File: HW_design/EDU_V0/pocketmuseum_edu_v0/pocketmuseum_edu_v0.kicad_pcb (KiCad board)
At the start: 4 copper layers, 96.8 x 51 mm, 106 parts, among them J101 USB_C_Receptacle_USB2.0_16P, J102 JST PH S2B, J201 TF-015, J205 BM04B-SRSS-TB, J206 BM04B-SRSS-TB, Q301 BSS138, Q302 BSS138, Q303 BSS138, SW101 PTS810SJG250, SW201 PTS810SJG250, U101 BQ24040, U102 APX803-29SAG, U103 AP2112K-3.3, U104 AP2112K-1.8, U201 ESP32-C6-MINI-1/U, U301 ICM-20948, U302 ICP20100, U303 BH1750FVI, U304 T3902

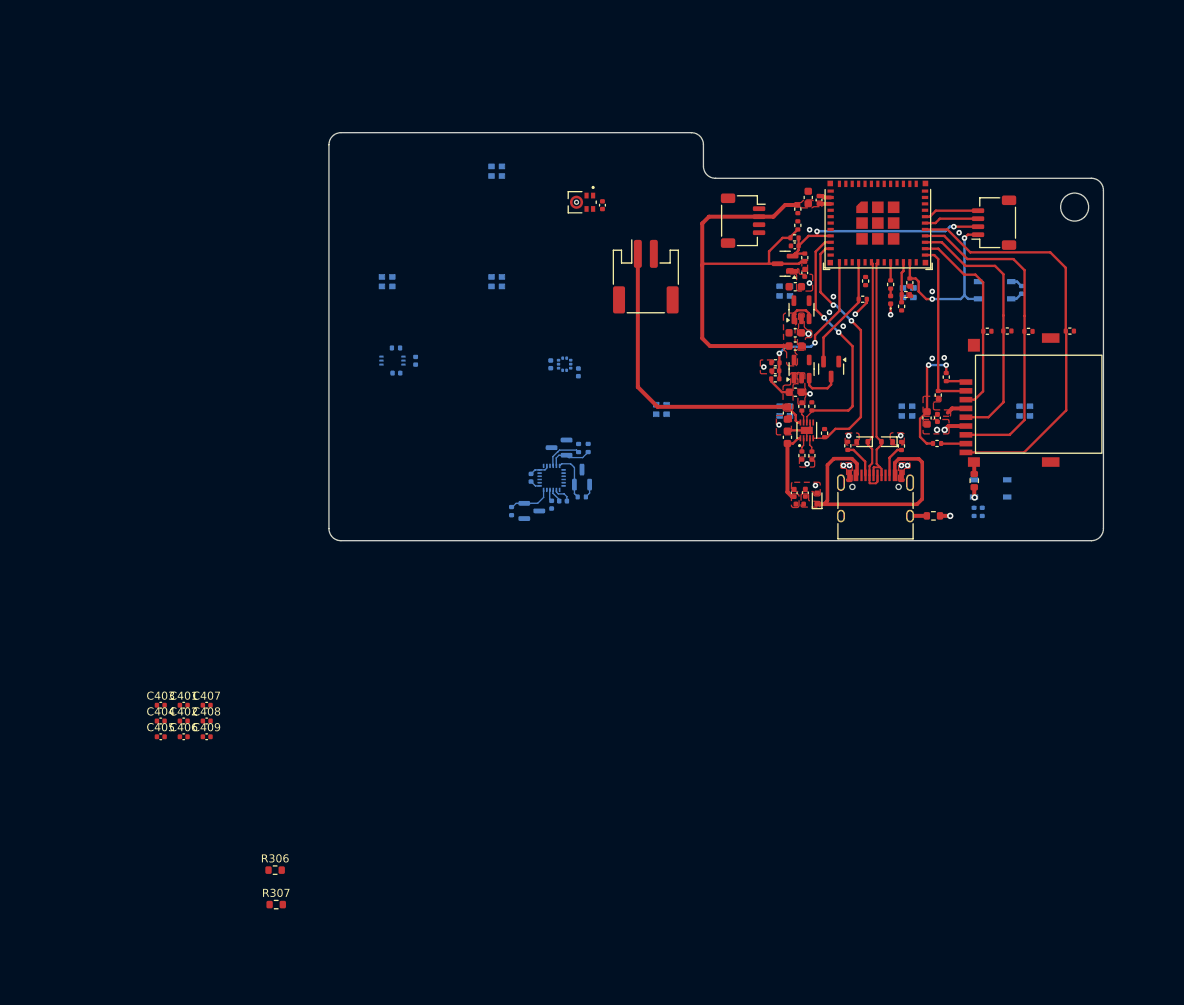
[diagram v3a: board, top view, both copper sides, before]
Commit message: EDU V0 PCB Placement Complete
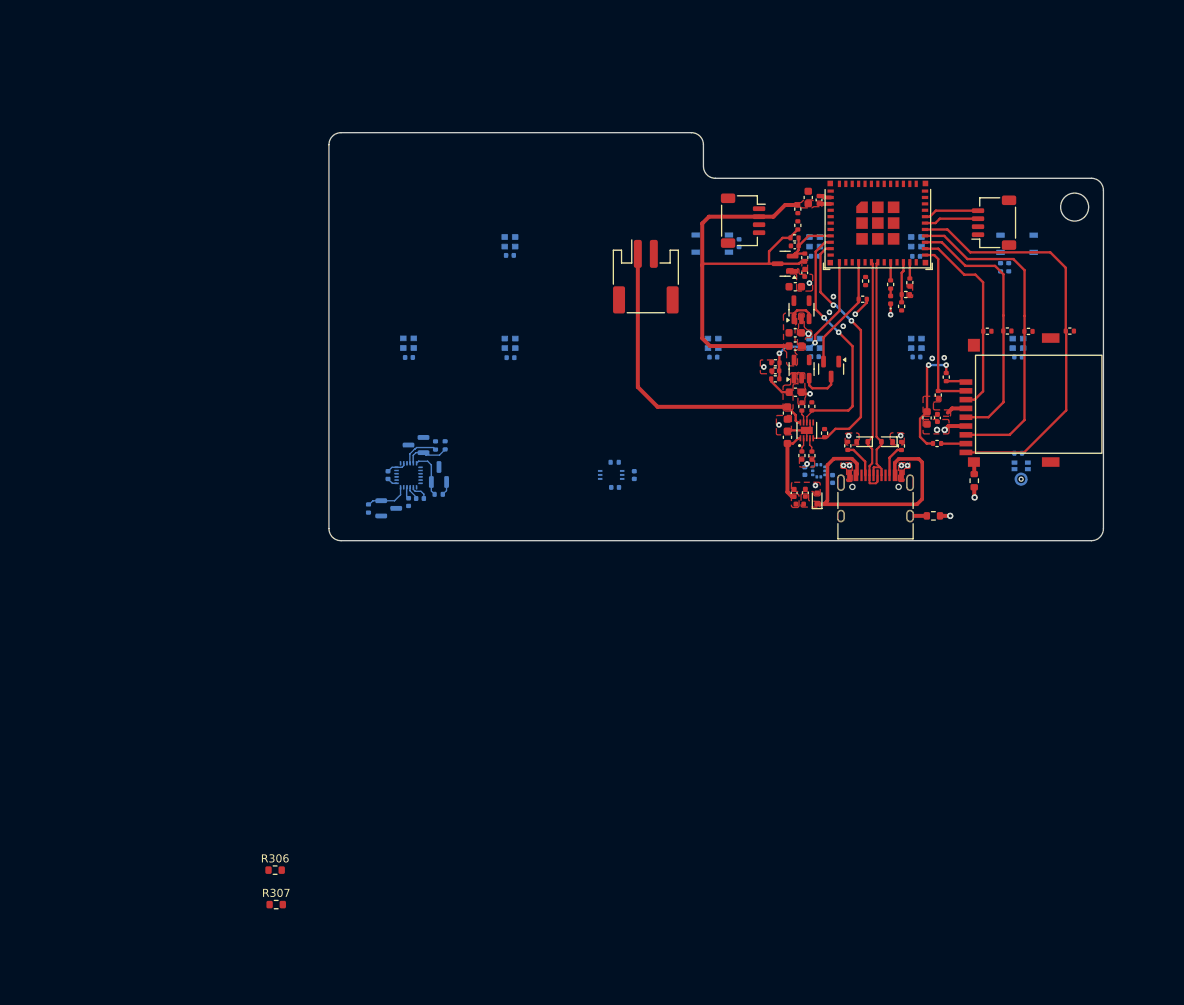
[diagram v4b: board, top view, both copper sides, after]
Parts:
- C308, C401, C402, C403, C404, C405, C406, C407, C408, C409, U304: moved to B.Cu
- moved C409 112.0 mm to (183.9, 93.8), turned to 180 degrees
- moved C401 107.4 mm to (171.2, 81.3), turned to 180 degrees
- moved C408 99.7 mm to (171.2, 93.8), turned to 180 degrees
- moved C402 98.0 mm to (158.5, 81.2), turned to 180 degrees
- moved C407 87.6 mm to (158.5, 93.8), turned to 180 degrees
- moved C406 81.5 mm to (145.8, 93.9), turned to 180 degrees
- moved D409 79.2 mm to (183.3, 96.3)
- moved C403 71.2 mm to (120.4, 81.1), turned to 180 degrees
- moved U304 64.5 mm to (184.3, 108.4), turned to 180 degrees
- moved C405 64.5 mm to (120.5, 93.9), turned to 180 degrees
- moved C308 60.5 mm to (183.9, 105.9), turned to 0 degrees
- moved C404 55.0 mm to (107.8, 93.9), turned to 180 degrees
- moved D403 54.0 mm to (119.8, 83.6)
- moved D408 53.0 mm to (170.6, 96.3)
- moved D404 47.8 mm to (107.1, 96.3)
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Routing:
- net /MCU/STRAP_GPIO_9: track 23.3 -> 2.03 mm, vias 2 -> 0
- net CHIP_PU: track 29.7 -> 8.77 mm, vias 2 -> 0
- net GND: track 22.9 -> 21.4 mm, vias 27 -> 24

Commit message: EDUV0 HW Complete Placement
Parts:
- added H2: MountingHole, MountingHole:MountingHole_3.2mm_M3, F.Cu at (101.2, 113.4)
- added H3: MountingHole, MountingHole:MountingHole_3.2mm_M3, F.Cu at (101.2, 69.2)
- added H4: MountingHole, MountingHole:MountingHole_3.2mm_M3, F.Cu at (191.2, 113.3)
- H1: footprint MountingHole:MountingHole_3.5mm -> MountingHole:MountingHole_3.2mm_M3
- moved SW101 50.7 mm to (133.9, 71.0), turned to -90 degrees
- moved R112 47.2 mm to (136.8, 72.0), turned to 0 degrees
- moved R111 45.9 mm to (136.8, 73.0), turned to 180 degrees
- moved SW201 38.1 mm to (183.8, 80.1), turned to 90 degrees
- moved C203 35.0 mm to (183.9, 83.4), turned to 0 degrees
- moved R304 9.22 mm to (111.9, 113.0), turned to 180 degrees
- moved R301 8.38 mm to (104.0, 103.5), turned to 0 degrees
- moved R305 7.05 mm to (104.1, 104.7), turned to 0 degrees
- moved Q303 7.03 mm to (111.9, 110.5), turned to 90 degrees
- moved R302 6.88 mm to (110.2, 104.3), turned to -90 degrees
- moved Q301 5.77 mm to (107.7, 104.2), turned to 180 degrees
- moved C303 5.21 mm to (111.1, 108.0), turned to 180 degrees
- moved Q302 5.18 mm to (104.0, 107.1), turned to -90 degrees
- moved C301 5.16 mm to (110.7, 106.6), turned to -90 degrees
- moved C302 3.28 mm to (107.8, 110.6), turned to 0 degrees
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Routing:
- net BATT_VOLT_FDBCK: track 19.5 -> 10.5 mm, vias 2 -> 1

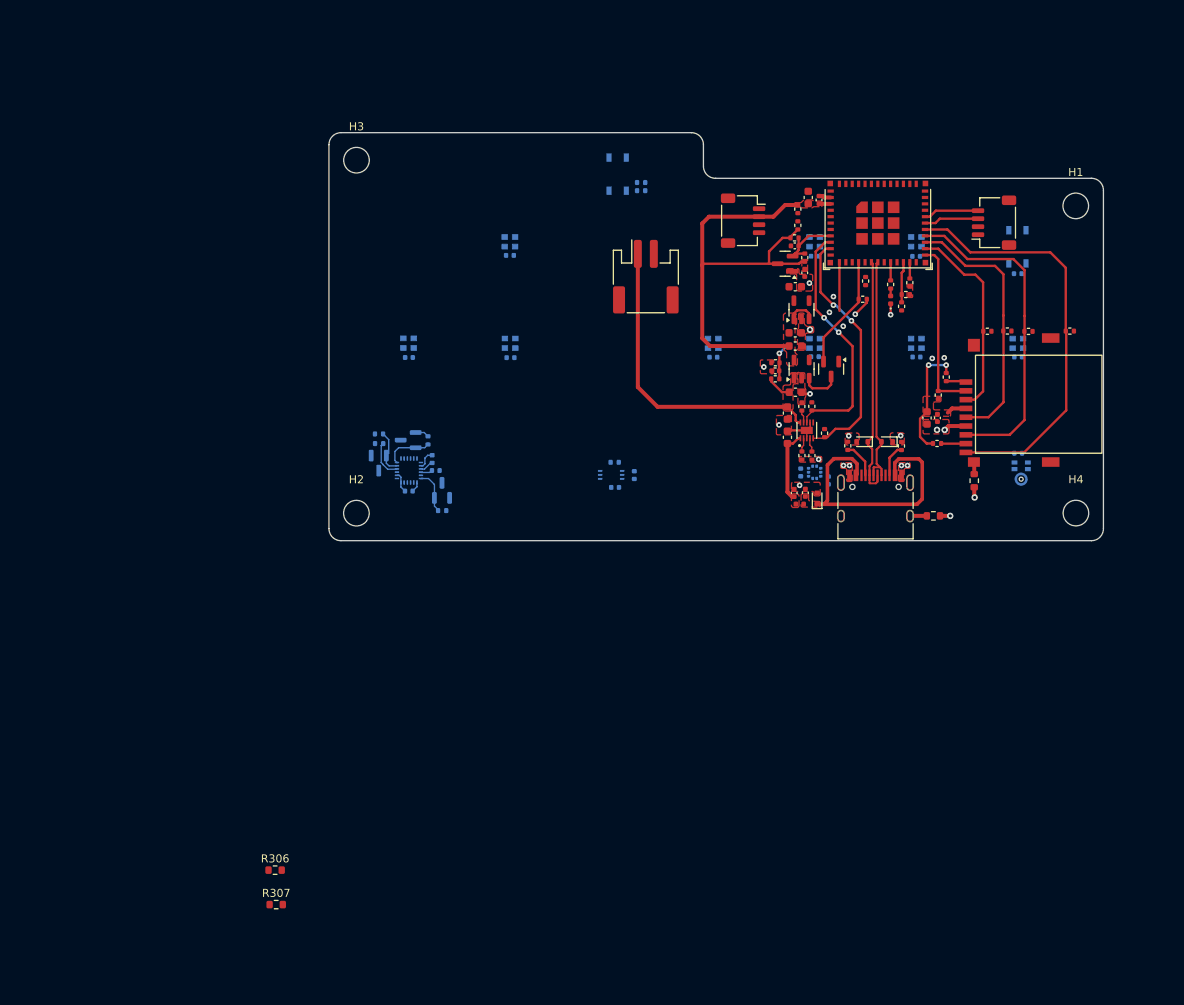
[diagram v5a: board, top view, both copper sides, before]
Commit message: EDUV0 added TP n routing in progress
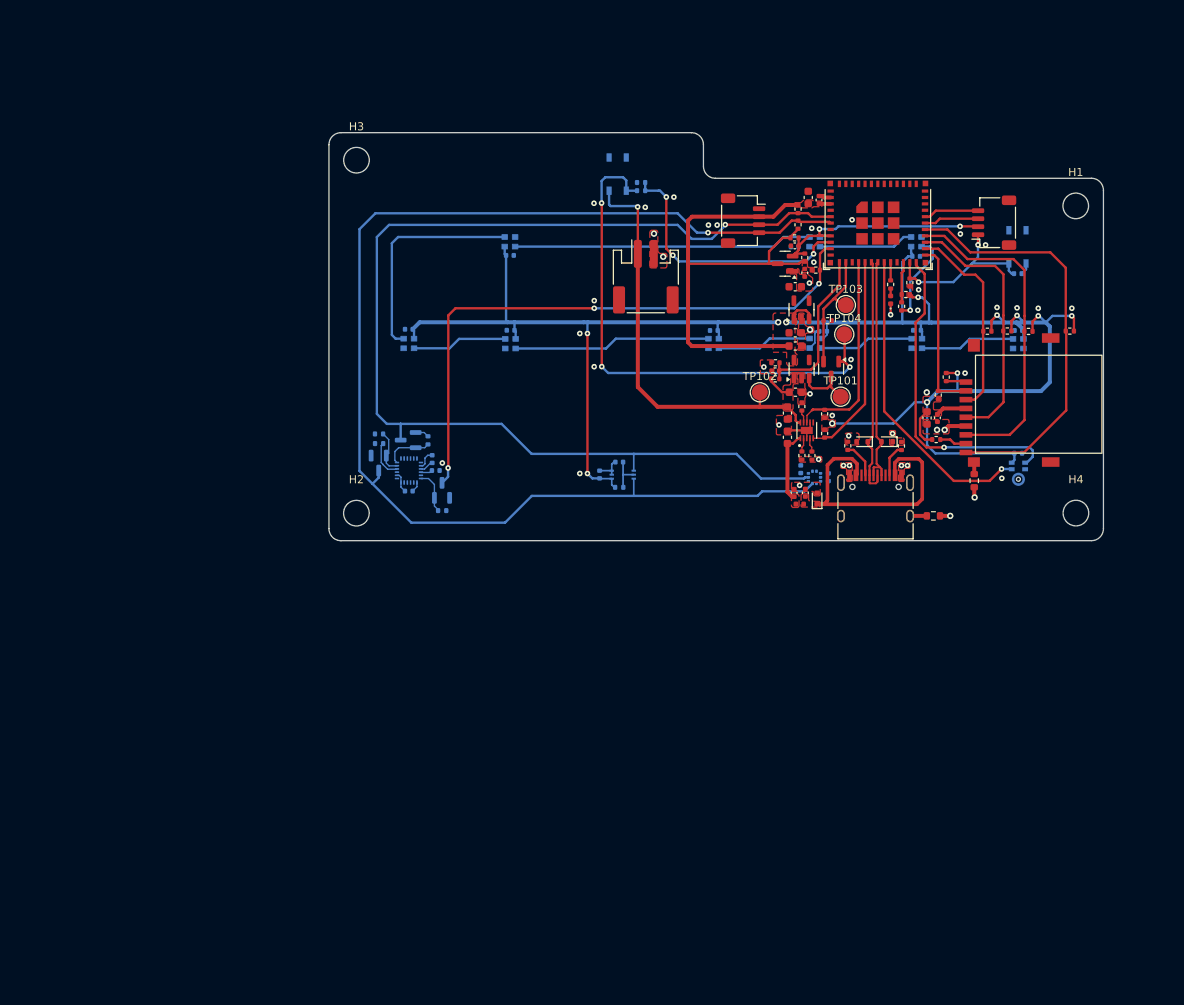
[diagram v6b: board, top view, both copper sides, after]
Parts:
- removed R306, R307: 0R, Resistor_SMD:R_0603_1608Metric
- added TP101: TestPoint, TestPoint:TestPoint_Pad_D2.0mm, F.Cu at (161.8, 98.8)
- added TP102: TestPoint, TestPoint:TestPoint_Pad_D2.0mm, F.Cu at (151.7, 98.2)
- added TP103: TestPoint, TestPoint:TestPoint_Pad_D2.0mm, F.Cu at (162.4, 87.3)
- added TP104: TestPoint, TestPoint:TestPoint_Pad_D2.0mm, F.Cu at (162.2, 91.0)
- moved D407 8.52 mm to (159.2, 87.9), turned to 0 degrees
- moved D406 8.50 mm to (146.5, 88.0), turned to 0 degrees
- moved D408 8.50 mm to (171.9, 88.0), turned to 0 degrees
- moved D409 8.47 mm to (184.6, 88.0), turned to 0 degrees
- moved D404 8.47 mm to (108.4, 88.0), turned to 0 degrees
- moved D405 8.46 mm to (121.1, 88.0), turned to 0 degrees
- moved R303 6.37 mm to (158.7, 83.0), turned to 0 degrees
- moved R113 5.14 mm to (160.1, 89.3)
- moved C306 4.34 mm to (131.6, 108.5), turned to 90 degrees
- moved C305 3.73 mm to (156.8, 107.9), turned to -90 degrees
- moved C404 3.53 mm to (107.8, 90.4), turned to 0 degrees
- moved C304 3.51 mm to (160.2, 108.9), turned to 90 degrees
- moved C405 3.42 mm to (120.5, 90.5), turned to 0 degrees
- moved C408 3.34 mm to (171.3, 90.5), turned to 0 degrees
- moved C406 3.34 mm to (145.9, 90.5), turned to 0 degrees
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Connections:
- U201 pad 10: BATT_POWOK_FDBCK -> MEMS_INT
- U201 pad 13: BATT_SW_FDBCK -> BATT_ATTCH_CMD
- U201 pad 15: BATT_ATTCH_CMD -> BATT_CHRG_FDBCK
- U201 pad 16: MEMS_INT -> BATT_POWOK_FDBCK
- U201 pad 5: I2C_SCL -> I2C_SDA
- U201 pad 6: I2C_SDA -> I2C_SCL
- U201 pad 9: BATT_CHRG_FDBCK -> BATT_SW_FDBCK
- U302 pad 2: Net-(U302-SCL) -> I2C_SCL
- U302 pad 4: Net-(U302-SDA) -> I2C_SDA
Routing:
- net +3V3: track 80.0 -> 293.7 mm, vias 2 -> 12
- net I2C_SCL: track 0.00 -> 157.1 mm, vias 0 -> 1
- net I2C_SDA: track 0.00 -> 143.2 mm, vias 0 -> 1
- net MEMS_INT: track 0.00 -> 74.6 mm, vias 0 -> 3
- net /Power/BATT_SW_CMD: track 0.00 -> 66.2 mm, vias 0 -> 3
- net I2S_DAT: track 0.00 -> 40.1 mm, vias 0 -> 1
- net I2S_CLK: track 0.00 -> 38.8 mm, vias 0 -> 1
- net /Feedback/WS2812B_Chain2: track 0.00 -> 37.3 mm
- net BATT_SW_FDBCK: track 0.00 -> 33.2 mm, vias 0 -> 3
- net /Feedback/WS2812B_Chain3: track 0.00 -> 27.6 mm
- net /Feedback/WS2812B_Chain5: track 0.00 -> 24.6 mm
- net CHIP_PU: track 8.77 -> 31.0 mm, vias 0 -> 2
- net /MCU/STRAP_GPIO_9: track 2.03 -> 21.2 mm, vias 0 -> 2
- net VBAT_ALW_ON: track 42.3 -> 55.4 mm, vias 0 -> 1
- net /Feedback/WS2812B_Chain7: track 0.00 -> 11.9 mm
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
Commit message: EDUV0 signals & 3V3 traces COMPLETE
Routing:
- net +3V3: track 293.7 -> 321.2 mm, vias 12 -> 13
- net GND: track 27.8 -> 31.9 mm, vias 46 -> 47
